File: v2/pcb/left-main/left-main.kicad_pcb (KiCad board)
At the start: 2 copper layers, 83 x 79 mm, 33 parts, among them J1 Conn_01x10, SW1 SW_Push, SW10 SW_Push, SW11 SW_Push, SW12 SW_Push, SW13 SW_Push, SW14 SW_Push, SW15 SW_Push, SW16 SW_Push, SW2 SW_Push, SW3 SW_Push, SW4 SW_Push, SW5 SW_Push, SW6 SW_Push, SW7 SW_Push, SW8 SW_Push, SW9 SW_Push

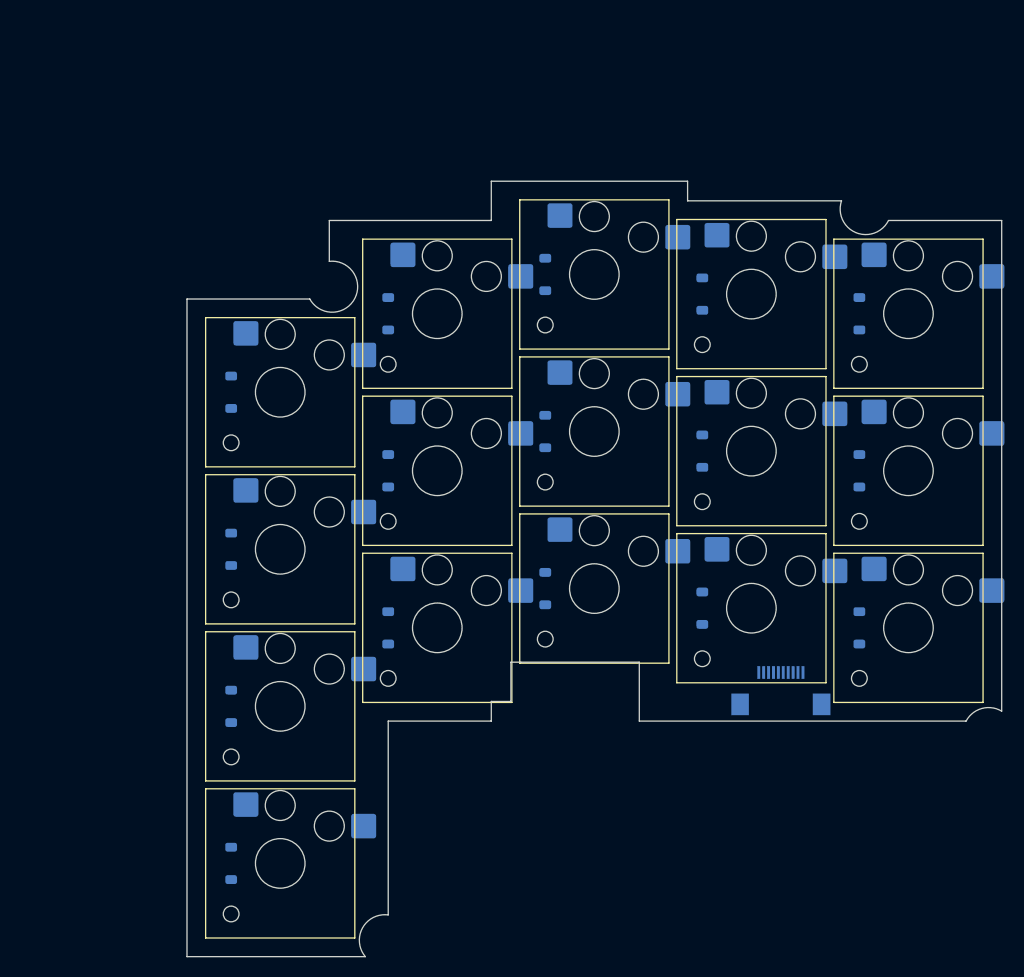
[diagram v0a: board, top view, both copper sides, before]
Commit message: feat: add left main pcb
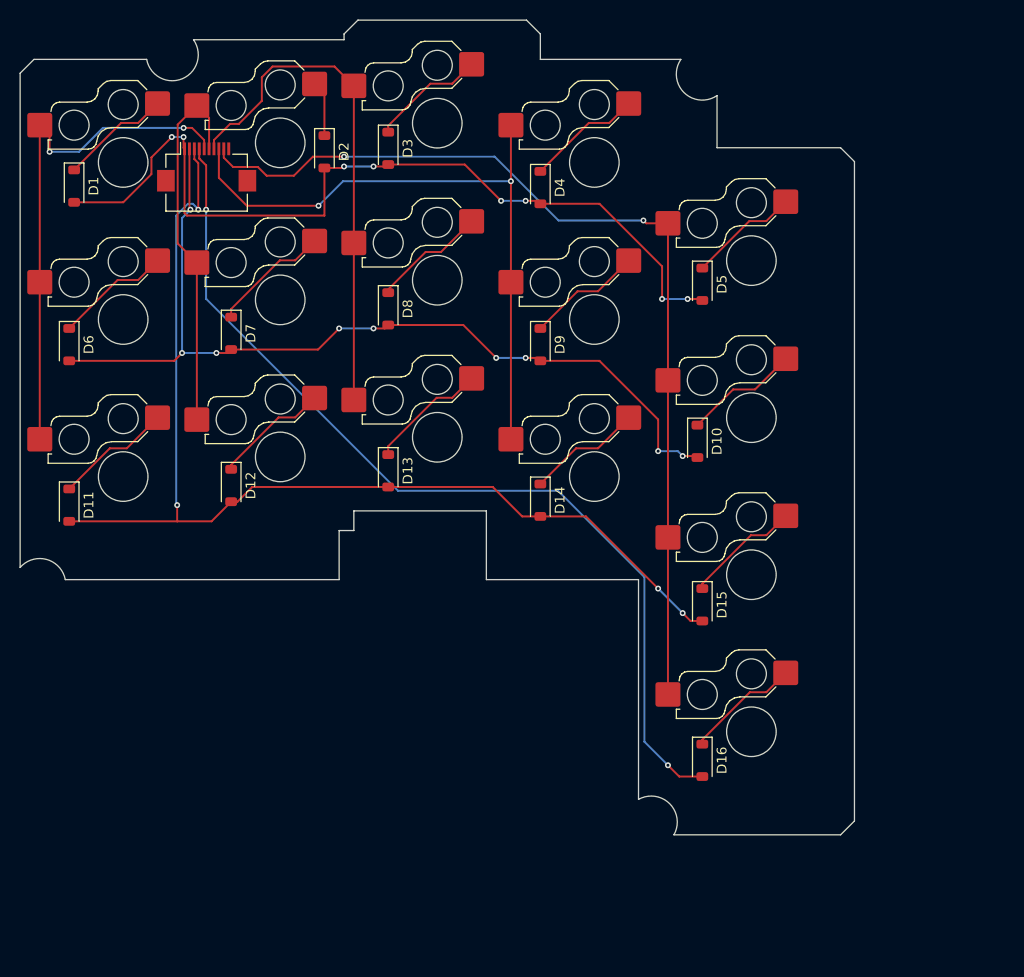
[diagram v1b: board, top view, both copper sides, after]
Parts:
- D1, D10, D11, D12, D13, D14, D15, D16, D2, D3, D4, D5, D6, D7, D8, D9, J1: moved to F.Cu
- SW1, SW10, SW11, SW12, SW13, SW14, SW15, SW16, SW2, SW3, SW4, SW5, SW6, SW7, SW8, SW9: moved to B.Cu
- moved D6 81.5 mm to (112.5, 94.7)
- moved SW1 81.5 mm to (118.0, 76.1), turned to 180 degrees
- moved SW11 81.5 mm to (118.0, 108.1), turned to 180 degrees
- moved SW6 81.5 mm to (118.0, 92.1), turned to 180 degrees
- moved D11 81.5 mm to (112.5, 111.0)
- moved D1 81.0 mm to (113.0, 78.5)
- moved J1 79.2 mm to (126.5, 76.5), turned to 0 degrees
- moved SW12 50.4 mm to (134.0, 106.1), turned to 180 degrees
- moved SW2 50.4 mm to (134.0, 74.1), turned to 180 degrees
- moved SW7 50.4 mm to (134.0, 90.1), turned to 180 degrees
- moved SW10 49.8 mm to (182.0, 102.1), turned to 180 degrees
- moved SW15 49.8 mm to (182.0, 118.1), turned to 180 degrees
- moved SW16 49.8 mm to (182.0, 134.1), turned to 180 degrees
- moved SW5 49.8 mm to (182.0, 86.1), turned to 180 degrees
- moved D12 49.6 mm to (129.0, 109.0)
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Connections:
- J1 pad 1: /COL4 -> /ROW0
- J1 pad 10: /ROW3 -> unconnected-(J1-Pin_10-Pad10)
- J1 pad 2: /COL3 -> /ROW1
- J1 pad 3: /COL2 -> /ROW2
- J1 pad 4: /COL1 -> /ROW3
- J1 pad 6: /ROW2 -> /COL1
- J1 pad 7: /ROW1 -> /COL2
- J1 pad 8: /ROW0 -> /COL3
- J1 pad 9: GND -> /COL4
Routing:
- net /ROW2: track 0.00 -> 112.2 mm, vias 0 -> 4
- net /COL4: track 0.00 -> 98.5 mm, vias 0 -> 2
- net /ROW3: track 0.00 -> 96.1 mm, vias 0 -> 2
- net /ROW1: track 0.00 -> 94.2 mm, vias 0 -> 9
- net /ROW0: track 0.00 -> 88.2 mm, vias 0 -> 8
- net /COL3: track 0.00 -> 66.9 mm, vias 0 -> 2
- net /COL0: track 0.00 -> 53.3 mm, vias 0 -> 2
- net /COL2: track 0.00 -> 52.5 mm
- net /COL1: track 0.00 -> 38.5 mm
- net Net-(D13-K): track 0.00 -> 12.2 mm
- net Net-(D7-K): track 0.00 -> 12.2 mm
- net Net-(D11-K): track 0.00 -> 12.0 mm
- net Net-(D4-K): track 0.00 -> 11.9 mm
- net Net-(D6-K): track 0.00 -> 11.9 mm
- net Net-(D9-K): track 0.00 -> 11.9 mm
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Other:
- board size 83 x 79 mm -> 85 x 83 mm
